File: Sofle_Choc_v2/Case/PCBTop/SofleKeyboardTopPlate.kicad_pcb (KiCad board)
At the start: 2 copper layers, 143.4 x 111.8 mm, 34 parts, among them SW2 KEY_SWITCH

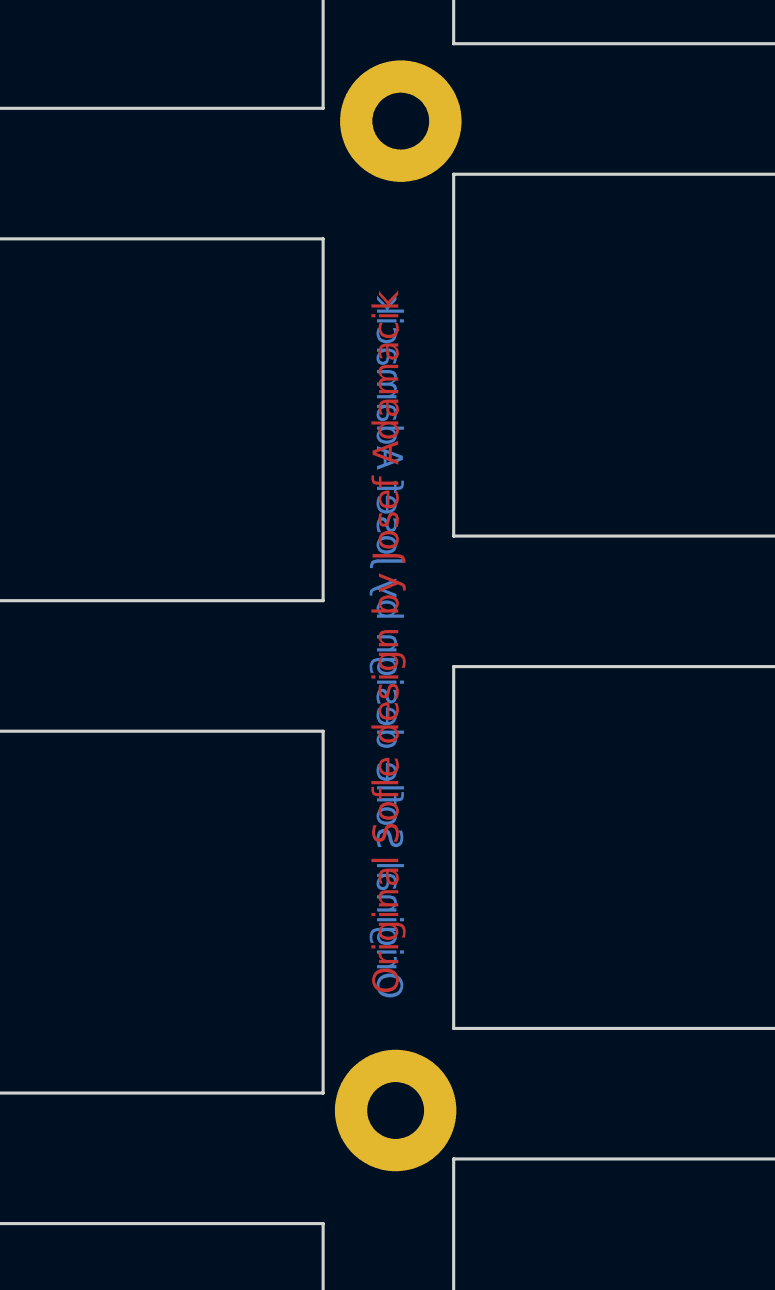
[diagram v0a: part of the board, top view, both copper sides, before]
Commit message: Tweak top layer silkscreen, build production files
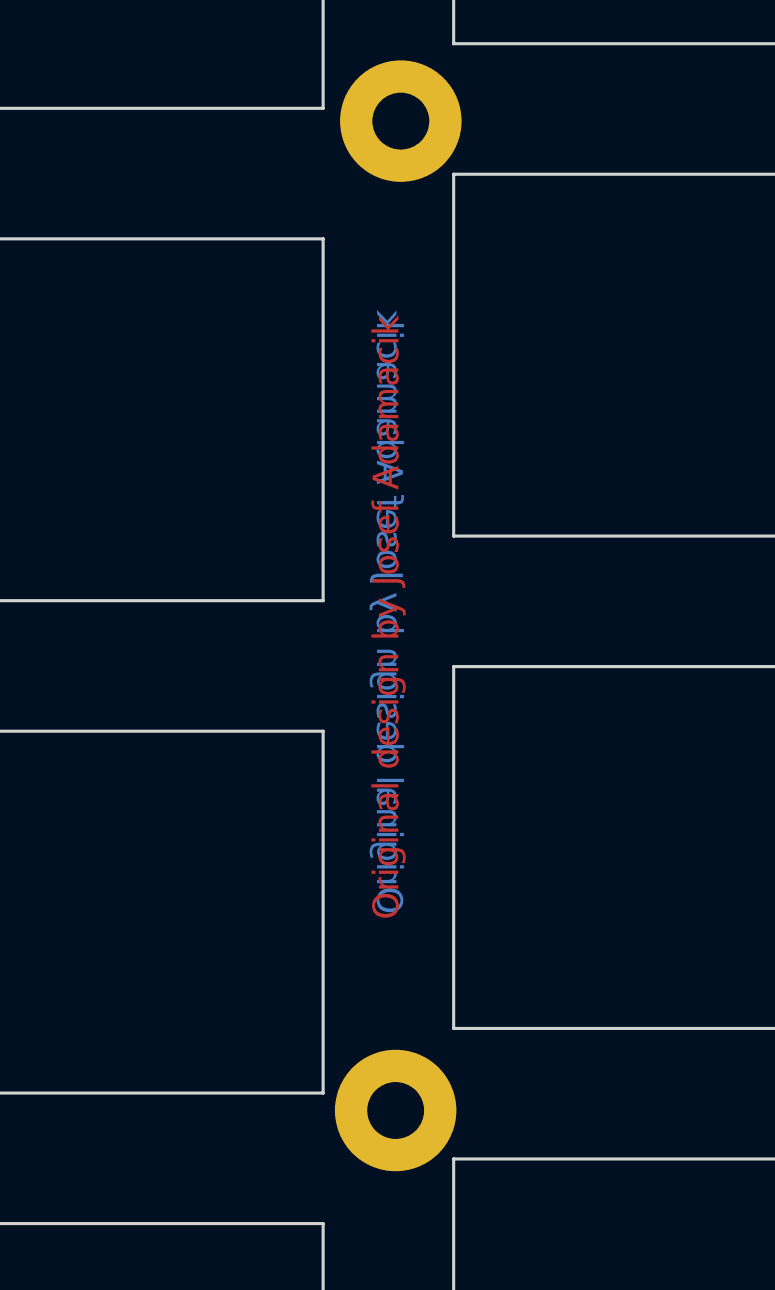
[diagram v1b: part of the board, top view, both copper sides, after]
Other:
- board text added: "Original design by Josef Adamacik"
- board text removed: "Original Sofle design by Josef Adamacik"
